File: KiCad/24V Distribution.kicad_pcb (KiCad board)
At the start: 4 copper layers, 101.6 x 101.6 mm, 10 parts, among them J201 Conn_02x32_Odd_Even, J202 Conn_02x20_Odd_Even

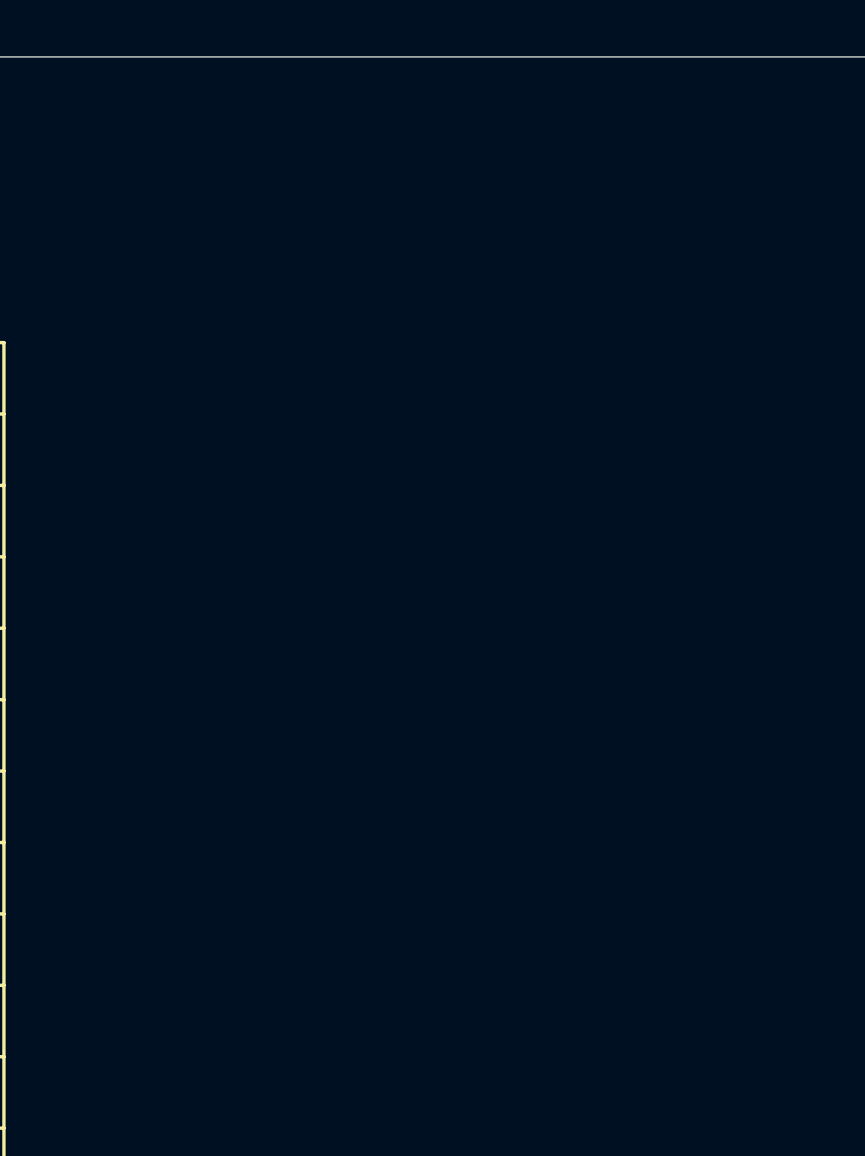
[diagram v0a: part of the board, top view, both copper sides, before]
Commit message: Updated PCB and schematic and changed datasheet
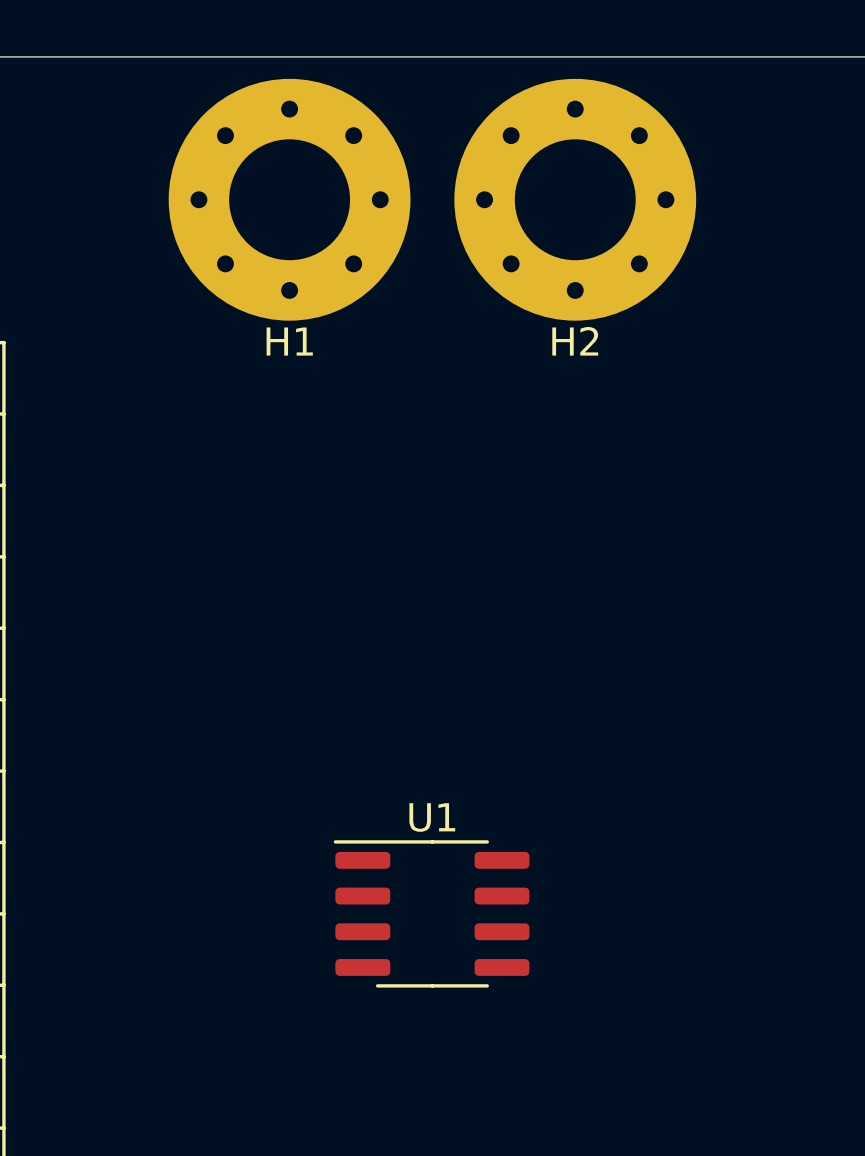
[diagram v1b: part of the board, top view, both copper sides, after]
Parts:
- added H1: +24V, MountingHole:MountingHole_4.3mm_M4_Pad_Via, F.Cu at (119.5, 39.0)
- added H2: GND, MountingHole:MountingHole_4.3mm_M4_Pad_Via, F.Cu at (129.7, 39.0)
- added U1: MC34063AD, Package_SO:SOIC-8_3.9x4.9mm_P1.27mm, F.Cu at (124.6, 64.4)
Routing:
- added copper zone on In2.Cu, net V+
- removed copper zone on In2.Cu, net (none)
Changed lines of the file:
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@@
   (net 88 "TX2")
   (net 89 "RX2")
+  (net 90 "unconnected-(U1-Pad1)")
+  (net 91 "unconnected-(U1-Pad2)")
+  (net 92 "unconnected-(U1-Pad3)")
+  (net 93 "unconnected-(U1-Pad4)")
+  (net 94 "unconnected-(U1-Pad5)")
+  (net 95 "unconnected-(U1-Pad6)")
+  (net 96 "unconnected-(U1-Pad7)")
+  (net 97 "unconnected-(U1-Pad8)")
   (footprint "MEP_TEMPLATE:Scope_GND" locked (layer "F.Cu")
     (at 191.91 50.47 90)
@@
     )
   )
+  (footprint "Package_SO:SOIC-8_3.9x4.9mm_P1.27mm" (layer "F.Cu")
+    (at 124.6 64.44)
+    (descr "SOIC, 8 Pin (JEDEC MS-012AA, https://www.analog.com/media/en/package-pcb-resources/package/pkg_pdf/soic_narrow-r/r_8.pdf), generated with kicad-footprint-generator ipc_gullwing_generator.py")
+    (tags "SOIC SO")
+    (property "Sheetfile" "24V Distribution.kicad_sch")
+    (property "Sheetname" "")
+    (attr smd)
+    (fp_text reference "U1" (at 0 -3.4) (layer "F.SilkS")
+      (effects (font (size 1 1) (thickness 0.15)))
+    )
+    (fp_text value "MC34063AD" (at 0 3.4) (layer "F.Fab")
+      (effects (font (size 1 1) (thickness 0.15)))
+    )
+    (fp_text user "${REFERENCE}" (at 0 0) (layer "F.Fab")
+      (effects (font (size 0.98 0.98) (thickness 0.15)))
+    )
+    (fp_line (start 0 -2.56) (end -3.45 -2.56) (layer "F.SilkS") (width 0.12))
+    (fp_line (start 0 2.56) (end 1.95 2.56) (layer "F.SilkS") (width 0.12))
+    (fp_line (start 0 2.56) (end -1.95 2.56) (layer "F.SilkS") (width 0.12))
+    (fp_line (start 0 -2.56) (end 1.95 -2.56) (layer "F.SilkS") (width 0.12))
+    (fp_line (start -3.7 2.7) (end 3.7 2.7) (layer "F.CrtYd") (width 0.05))
+    (fp_line (start 3.7 2.7) (end 3.7 -2.7) (layer "F.CrtYd") (width 0.05))
+    (fp_line (start 3.7 -2.7) (end -3.7 -2.7) (layer "F.CrtYd") (width 0.05))
+    (fp_line (start -3.7 -2.7) (end -3.7 2.7) (layer "F.CrtYd") (width 0.05))
+    (fp_line (start 1.95 -2.45) (end 1.95 2.45) (layer "F.Fab") (width 0.1))
+    (fp_line (start -1.95 2.45) (end -1.95 -1.475) (layer "F.Fab") (width 0.1))
+    (fp_line (start -0.975 -2.45) (end 1.95 -2.45) (layer "F.Fab") (width 0.1))
+    (fp_line (start -1.95 -1.475) (end -0.975 -2.45) (layer "F.Fab") (width 0.1))
+    (fp_line (start 1.95 2.45) (end -1.95 2.45) (layer "F.Fab") (width 0.1))
+    (pad "1" smd roundrect locked (at -2.475 -1.905) (size 1.95 0.6) (layers "F.Cu" "F.Paste" "F.Mask") (roundrect_rratio 0.25)
+      (net 90 "unconnected-(U1-Pad1)") (pinfunction "SwC") (pintype "open_collector"))
+    (pad "2" smd roundrect locked (at -2.475 -0.635) (size 1.95 0.6) (layers "F.Cu" "F.Paste" "F.Mask") (roundrect_rratio 0.25)
+      (net 91 "unconnected-(U1-Pad2)") (pinfunction "SwE") (pintype "open_emitter"))
+    (pad "3" smd roundrect locked (at -2.475 0.635) (size 1.95 0.6) (layers "F.Cu" "F.Paste" "F.Mask") (roundrect_rratio 0.25)
+      (net 92 "unconnected-(U1-Pad3)") (pinfunction "TC") (pintype "passive"))
+    (pad "4" smd roundrect locked (at -2.475 1.905) (size 1.95 0.6) (layers "F.Cu" "F.Paste" "F.Mask") (roundrect_rratio 0.25)
+      (net 93 "unconnected-(U1-Pad4)") (pinfunction "GND") (pintype "power_in"))
+    (pad "5" smd roundrect locked (at 2.475 1.905) (size 1.95 0.6) (layers "F.Cu" "F.Paste" "F.Mask") (roundrect_rratio 0.25)
+      (net 94 "unconnected-(U1-Pad5)") (pinfunction "Vfb") (pintype "input"))
+    (pad "6" smd roundrect locked (at 2.475 0.635) (size 1.95 0.6) (layers "F.Cu" "F.Paste" "F.Mask") (roundrect_rratio 0.25)
+      (net 95 "unconnected-(U1-Pad6)") (pinfunction "Vin") (pintype "power_in"))
+    (pad "7" smd roundrect locked (at 2.475 -0.635) (size 1.95 0.6) (layers "F.Cu" "F.Paste" "F.Mask") (roundrect_rratio 0.25)
+      (net 96 "unconnected-(U1-Pad7)") (pinfunction "Ipk") (pintype "input"))
+    (pad "8" smd roundrect locked (at 2.475 -1.905) (size 1.95 0.6) (layers "F.Cu" "F.Paste" "F.Mask") (roundrect_rratio 0.25)
+      (net 97 "unconnected-(U1-Pad8)") (pinfunction "DC") (pintype "open_collector"))
+    (model "${KICAD6_3DMODEL_DIR}/Package_SO.3dshapes/SOIC-8_3.9x4.9mm_P1.27mm.wrl"
+      (offset (xyz 0 0 0))
+      (scale (xyz 1 1 1))
+      (rotate (xyz 0 0 0))
+    )
+  )
+  (footprint "MountingHole:MountingHole_4.3mm_M4_Pad_Via" (layer "F.Cu")
+    (at 129.68 39.04)
+    (descr "Mounting Hole 4.3mm, M4")
+    (tags "mounting hole 4.3mm m4")
+    (property "Sheetfile" "24V Distribution.kicad_sch")
+    (property "Sheetname" "")
+    (attr exclude_from_pos_files)
+    (fp_text reference "H2" (at 0 5.08) (layer "F.SilkS")
+      (effects (font (size 1 1) (thickness 0.15)))
+    )
+    (fp_text value "GND" (at 0 5.3) (layer "F.Fab")
+      (effects (font (size 1 1) (thickness 0.15)))
+    )
+    (fp_text user "${REFERENCE}" (at 0.3 0) (layer "F.Fab")
+      (effects (font (size 1 1) (thickness 0.15)))
+    )
+    (fp_circle (center 0 0) (end 4.3 0) (layer "Cmts.User") (width 0.15) (fill none))
+    (fp_circle (center 0 0) (end 4.55 0) (layer "F.CrtYd") (width 0.05) (fill none))
+    (pad "1" thru_hole circle locked (at 0 3.225) (size 0.9 0.9) (drill 0.6) (layers *.Cu *.Mask)
+      (net 1 "GND") (pinfunction "1") (pintype "input"))
+    (pad "1" thru_hole circle locked (at 2.280419 -2.280419) (size 0.9 0.9) (drill 0.6) (layers *.Cu *.Mask)
+      (net 1 "GND") (pinfunction "1") (pintype "input"))
+    (pad "1" thru_hole circle locked (at 0 0) (size 8.6 8.6) (drill 4.3) (layers *.Cu *.Mask)
+      (net 1 "GND") (pinfunction "1") (pintype "input"))
+    (pad "1" thru_hole circle locked (at -2.280419 2.280419) (size 0.9 0.9) (drill 0.6) (layers *.Cu *.Mask)
+      (net 1 "GND") (pinfunction "1") (pintype "input"))
+    (pad "1" thru_hole circle locked (at 2.280419 2.280419) (size 0.9 0.9) (drill 0.6) (layers *.Cu *.Mask)
+      (net 1 "GND") (pinfunction "1") (pintype "input"))
+    (pad "1" thru_hole circle locked (at 3.225 0) (size 0.9 0.9) (drill 0.6) (layers *.Cu *.Mask)
+      (net 1 "GND") (pinfunction "1") (pintype "input"))
+    (pad "1" thru_hole circle locked (at -2.280419 -2.280419) (size 0.9 0.9) (drill 0.6) (layers *.Cu *.Mask)
+      (net 1 "GND") (pinfunction "1") (pintype "input"))
+    (pad "1" thru_hole circle locked (at 0 -3.225) (size 0.9 0.9) (drill 0.6) (layers *.Cu *.Mask)
+      (net 1 "GND") (pinfunction "1") (pintype "input"))
+    (pad "1" thru_hole circle locked (at -3.225 0) (size 0.9 0.9) (drill 0.6) (layers *.Cu *.Mask)
+      (net 1 "GND") (pinfunction "1") (pintype "input"))
+  )
+  (footprint "MountingHole:MountingHole_4.3mm_M4_Pad_Via" (layer "F.Cu")
+    (at 119.52 39.04)
+    (descr "Mounting Hole 4.3mm, M4")
+    (tags "mounting hole 4.3mm m4")
+    (property "Sheetfile" "24V Distribution.kicad_sch")
+    (property "Sheetname" "")
+    (attr exclude_from_pos_files)
+    (fp_text reference "H1" (at 0 5.08) (layer "F.SilkS")
+      (effects (font (size 1 1) (thickness 0.15)))
+    )
+    (fp_text value "+24V" (at 0 5.3) (layer "F.Fab")
+      (effects (font (size 1 1) (thickness 0.15)))
+    )
+    (fp_text user "${REFERENCE}" (at 0.3 0) (layer "F.Fab")
+      (effects (font (size 1 1) (thickness 0.15)))
+    )
+    (fp_circle (center 0 0) (end 4.3 0) (layer "Cmts.User") (width 0.15) (fill none))
+    (fp_circle (center 0 0) (end 4.55 0) (layer "F.CrtYd") (width 0.05) (fill none))
+    (pad "1" thru_hole circle locked (at 2.280419 2.280419) (size 0.9 0.9) (drill 0.6) (layers *.Cu *.Mask)
+      (net 55 "V+") (pinfunction "1") (pintype "input"))
+    (pad "1" thru_hole circle locked (at 3.225 0) (size 0.9 0.9) (drill 0.6) (layers *.Cu *.Mask)
+      (net 55 "V+") (pinfunction "1") (pintype "input"))
+    (pad "1" thru_hole circle locked (at -2.280419 -2.280419) (size 0.9 0.9) (drill 0.6) (layers *.Cu *.Mask)
+      (net 55 "V+") (pinfunction "1") (pintype "input"))
+    (pad "1" thru_hole circle locked (at 0 3.225) (size 0.9 0.9) (drill 0.6) (layers *.Cu *.Mask)
+      (net 55 "V+") (pinfunction "1") (pintype "input"))
+    (pad "1" thru_hole circle locked (at 0 -3.225) (size 0.9 0.9) (drill 0.6) (layers *.Cu *.Mask)
+      (net 55 "V+") (pinfunction "1") (pintype "input"))
+    (pad "1" thru_hole circle locked (at -3.225 0) (size 0.9 0.9) (drill 0.6) (layers *.Cu *.Mask)
+      (net 55 "V+") (pinfunction "1") (pintype "input"))
+    (pad "1" thru_hole circle locked (at -2.280419 2.280419) (size 0.9 0.9) (drill 0.6) (layers *.Cu *.Mask)
+      (net 55 "V+") (pinfunction "1") (pintype "input"))
+    (pad "1" thru_hole circle locked (at 2.280419 -2.280419) (size 0.9 0.9) (drill 0.6) (layers *.Cu *.Mask)
+      (net 55 "V+") (pinfunction "1") (pintype "input"))
+    (pad "1" thru_hole circle locked (at 0 0) (size 8.6 8.6) (drill 4.3) (layers *.Cu *.Mask)
+      (net 55 "V+") (pinfunction "1") (pintype "input"))
+  )
   (footprint "Symbol:KiCad-Logo2_5mm_SilkScreen" locked (layer "B.Cu")
     (at 188.1 58.09 180)
@@
     )
   )
-  (zone locked (net 0) (net_name "") (layer "In2.Cu") (hatch edge 0.508)
+  (zone locked (net 1) (net_name "GND") (layer "In1.Cu") (hatch edge 0.508)
+    (connect_pads yes (clearance 0.508))
+    (min_thickness 0.254) (filled_areas_thickness no)
+    (fill yes (thermal_gap 0.508) (thermal_bridge_width 0.508))
+    (polygon
+      (pts
+        (xy 134.76 44.12)
+        (xy 124.6 44.12)
+        (xy 124.6 33.96)
+        (xy 134.76 33.96)
+      )
+    )
+  )
+  (zone locked (net 55) (net_name "V+") (layer "In2.Cu") (hatch edge 0.508)
     (connect_pads (clearance 0.508))
     (min_thickness 0.254) (filled_areas_thickness no)
@@
       )
     )
+  )
+  (zone locked (net 55) (net_name "V+") (layer "In2.Cu") (hatch edge 0.508)
+    (connect_pads yes (clearance 0.508))
+    (min_thickness 0.254) (filled_areas_thickness no)
+    (fill yes (thermal_gap 0.508) (thermal_bridge_width 0.508))
+    (polygon
+      (pts
+        (xy 124.6 44.12)
+        (xy 114.44 44.12)
+        (xy 114.44 33.96)
+        (xy 124.6 33.96)
+      )
+    )

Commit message: Updated to MEPOS V0.2
updated pcb
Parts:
- removed H1: +24V, MountingHole:MountingHole_4.3mm_M4_Pad_Via
- removed H2: GND, MountingHole:MountingHole_4.3mm_M4_Pad_Via
- added +24V: +24V, MountingHole:MountingHole_4.3mm_M4_Pad_Via, F.Cu at (133.5, 29.5)
- added GND: GND, MountingHole:MountingHole_4.3mm_M4_Pad_Via, F.Cu at (156.3, 29.5)
- moved U1 20.3 mm to (124.6, 44.1)
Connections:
- net AGND renamed GNDA
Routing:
- added copper zone on B.Cu, net GND
- added copper zone on F.Cu, net GND
- added copper zone on B.Cu, net V+
- added copper zone on F.Cu, net V+
- removed copper zone on In2.Cu, net V+
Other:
- board size 101.6 x 101.6 mm -> 101.6 x 111.1 mm
- board text added: "GNDA"
- board text added: "MEPOS_V22.03.0.2"
- board text removed: "AGND"
- board text removed: "MEPOS_V21.12.0.1"

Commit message: Updated to MEPOS V0.3
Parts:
- removed +24V: +24V, MountingHole:MountingHole_4.3mm_M4_Pad_Via
- removed GND: GND, MountingHole:MountingHole_4.3mm_M4_Pad_Via
- removed OSHW_Logo: OSHW-Logo2_14.6x12mm_SilkScreen, Symbol:OSHW-Logo2_14.6x12mm_SilkScreen
- removed U1: MC34063AD, Package_SO:SOIC-8_3.9x4.9mm_P1.27mm
- moved KiCad_Logo 1.27 mm to (188.1, 59.4)
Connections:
- net GNDA renamed AGND
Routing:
- removed copper zone on B.Cu, net GND
- removed copper zone on F.Cu, net GND
- removed copper zone on B.Cu, net V+
- removed copper zone on F.Cu, net V+
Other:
- board size 101.6 x 111.1 mm -> 101.6 x 101.6 mm
- board text added: "LECTRONICS"
- board text added: "MEPOS_V22.04.0.3"
- board text added: "RIED"
- board text removed: "MEPOS_V22.03.0.2"
